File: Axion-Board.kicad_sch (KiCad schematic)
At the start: 76 parts, among them J1 USB_C_Receptacle_USB2.0, J14 QE2B, J15 RGB2, J16 RGB1, J17 QE1, J18 QE2, J19 USB Header, J2 SWD, J20 PS2 Header, J21 QE2A, J3 QE1A, J4 QE1B, J5 LED, J6 GPIO, J7 GPIO, Q1 BSS138, Q10 BSS138, Q11 BSS138, Q2 BSS138, Q3 BSS138, Q4 BSS138, Q5 BSS138, Q6 BSS138, Q7 BSS138, Q8 BSS138, Q9 BSS138, SW1 SW_Push, U1 W25Q128JVS, U2 USBLC6-2SC6, U3 RP2040, U4 XC6206PxxxMR-Regulator_Linear, U5 SN74HCT125DR, U6 78M05_TO252-3, Y1 12MHz

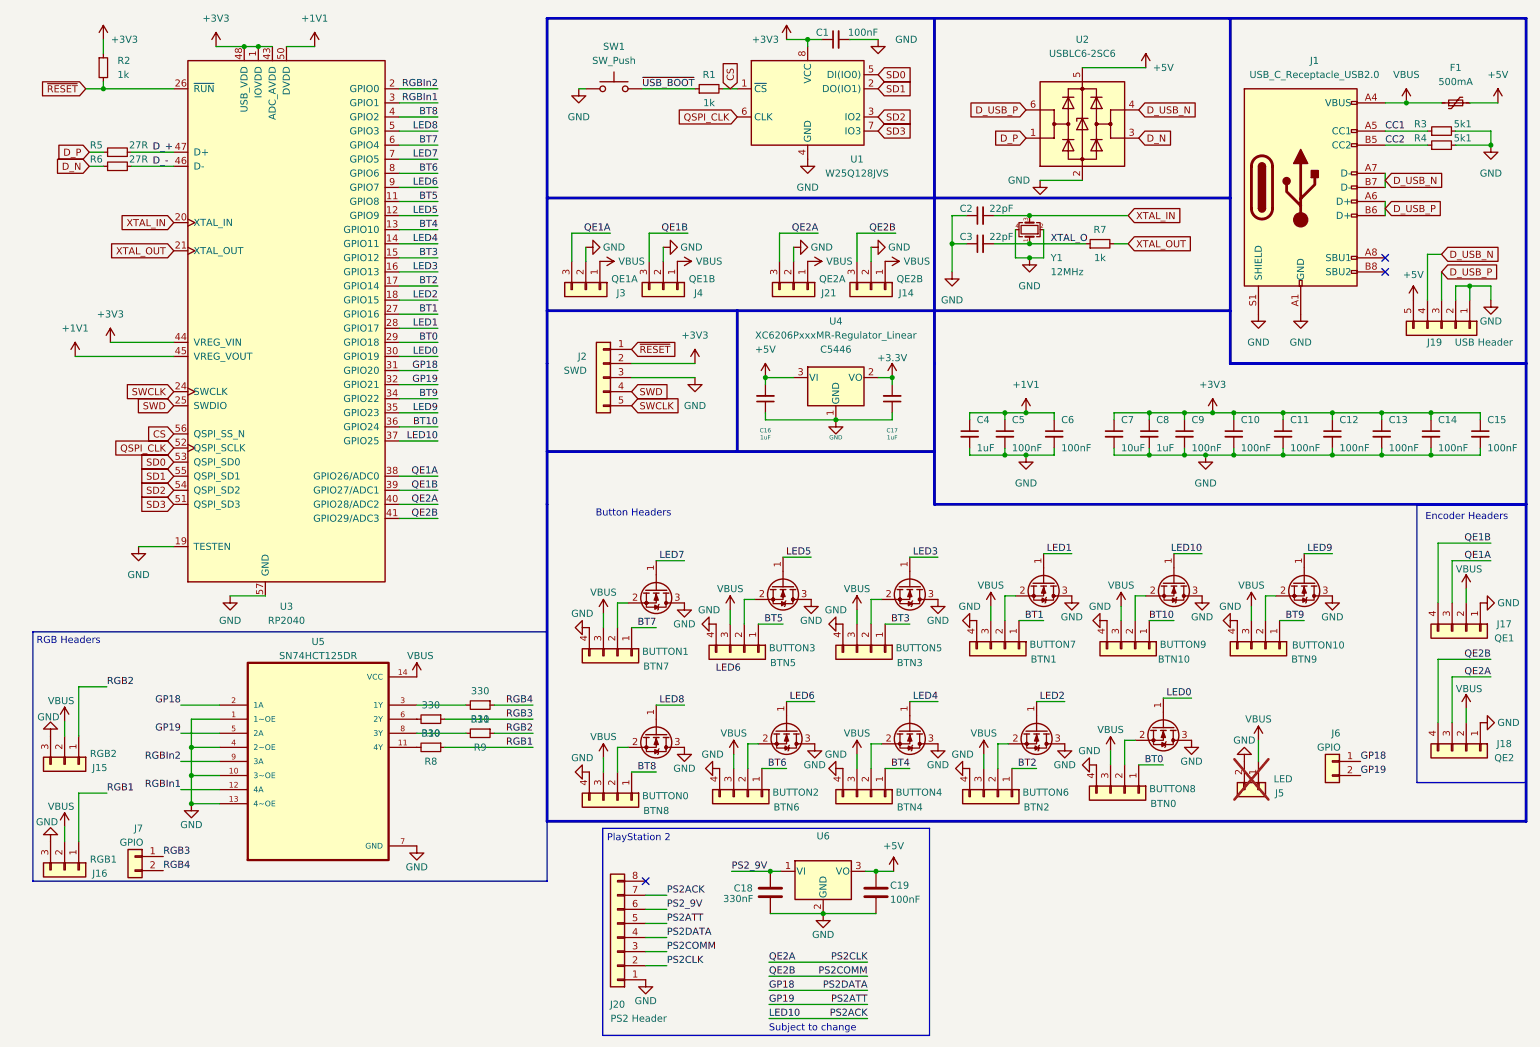
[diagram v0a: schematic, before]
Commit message: Fixed the mosfet wiring
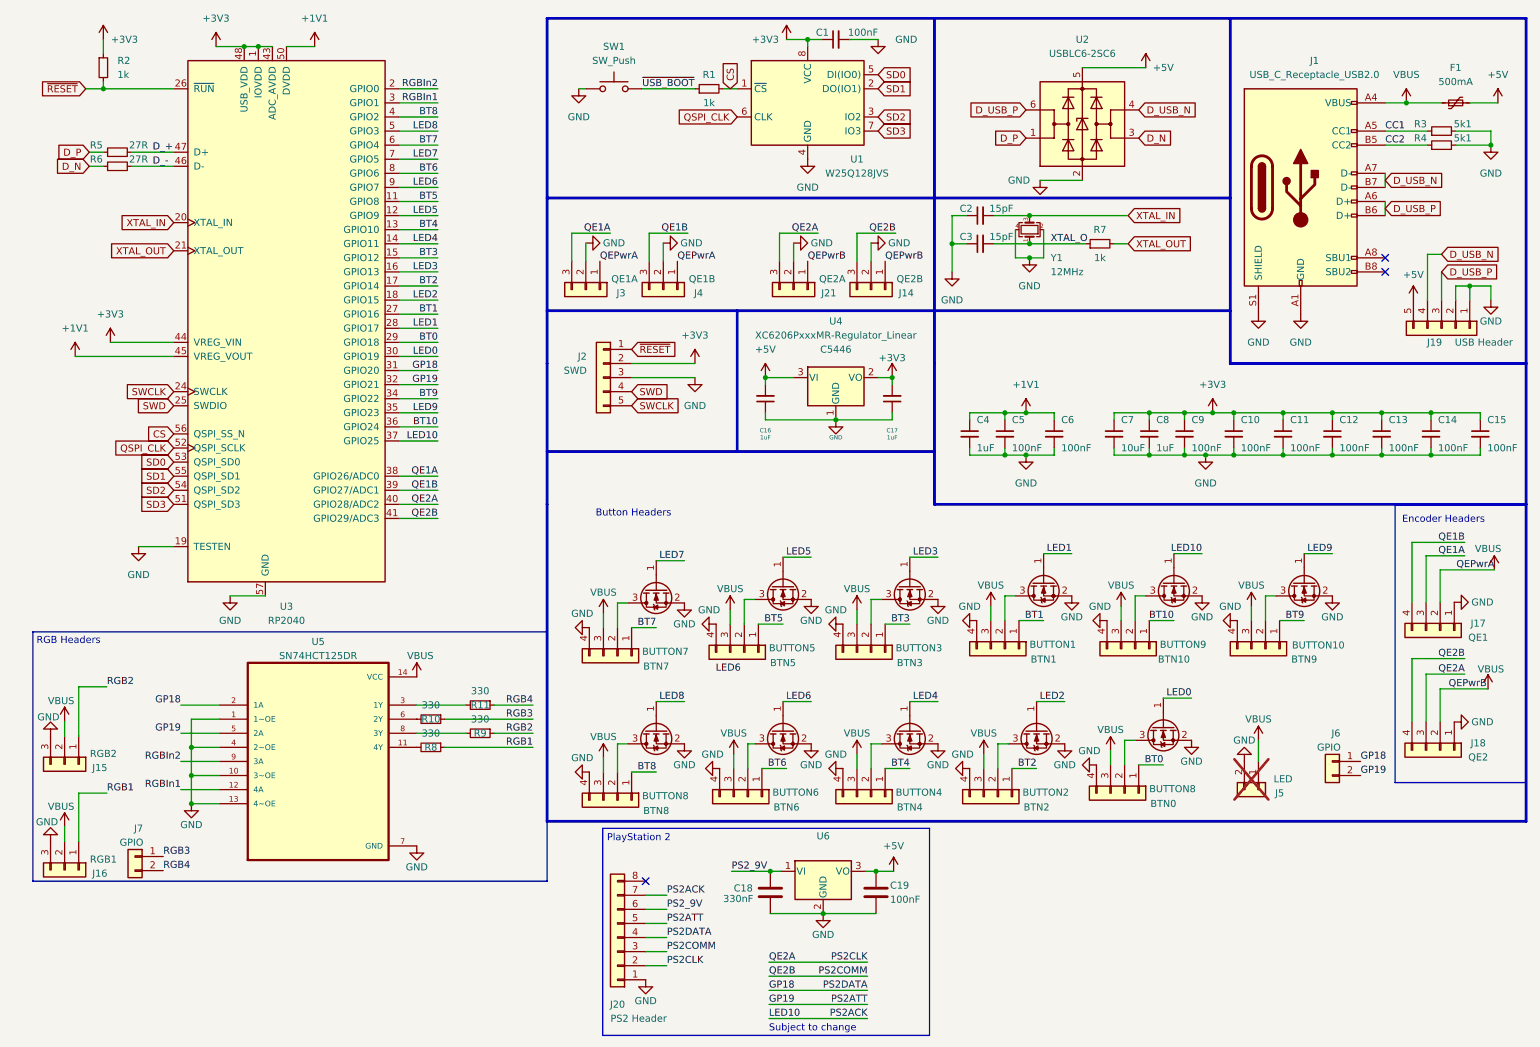
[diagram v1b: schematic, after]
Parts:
- BTN1: value BUTTON7 -> BUTTON1
- BTN2: value BUTTON6 -> BUTTON2
- BTN3: value BUTTON5 -> BUTTON3
- BTN5: value BUTTON3 -> BUTTON5
- BTN6: value BUTTON2 -> BUTTON6
- BTN7: value BUTTON1 -> BUTTON7
- BTN8: value BUTTON0 -> BUTTON8
- C2, C3: value 22pF -> 15pF
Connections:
- net GND: now also Q1.2 (S), Q10.2 (S), Q11.2 (S), Q2.2 (S), Q3.2 (S), Q4.2 (S), Q5.2 (S), Q6.2 (S), Q7.2 (S), Q8.2 (S), Q9.2 (S); no longer J1.B1 (GND), J1.B12 (GND), Q1.3 (D), Q10.3 (D), Q11.3 (D), Q2.3 (D), Q3.3 (D), Q4.3 (D), Q5.3 (D), Q6.3 (D), Q7.3 (D), Q8.3 (D), Q9.3 (D)
- net LED0: now also Q5.1 (G); no longer Q10.1 (G)
- net LED1: now also Q8.1 (G); no longer Q7.1 (G)
- net LED10: now also Q7.1 (G); no longer Q9.1 (G)
- net LED2: now also Q4.1 (G); no longer Q8.1 (G)
- net LED3: now also Q9.1 (G); no longer Q5.1 (G)
- net LED4: now also Q2.1 (G); no longer Q6.1 (G)
- net LED5: now also Q10.1 (G); no longer Q4.1 (G)
- net LED6: now also Q1.1 (G); no longer Q2.1 (G)
- net LED7: now also Q11.1 (G); no longer Q1.1 (G)
- net LED9: now also Q6.1 (G); no longer Q11.1 (G)
- net at BTN0.2 (Pin_2): now also Q5.3 (D); no longer Q10.2 (S)
- net at BTN9.2 (Pin_2): now also Q6.3 (D); no longer Q11.2 (S)
- net at BTN2.2 (Pin_2): now also Q4.3 (D); no longer Q8.2 (S)
- net at BTN5.2 (Pin_2): now also Q10.3 (D); no longer Q4.2 (S)
- net at BTN6.2 (Pin_2): now also Q1.3 (D); no longer Q2.2 (S)
- net at BTN8.2 (Pin_2): now also Q3.3 (D); no longer Q3.2 (S)
- net at BTN10.2 (Pin_2): now also Q7.3 (D); no longer Q9.2 (S)
- net at BTN4.2 (Pin_2): now also Q2.3 (D); no longer Q6.2 (S)
- net at BTN1.2 (Pin_2): now also Q8.3 (D); no longer Q7.2 (S)
- net at BTN7.2 (Pin_2): now also Q11.3 (D); no longer Q1.2 (S)
- net at BTN3.2 (Pin_2): now also Q9.3 (D); no longer Q5.2 (S)
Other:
- moved on the sheet: J17, J18

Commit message: Added turntable LED header
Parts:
- added J8: LED, Connector_JST:JST_XH_B2B-XH-A_1x02_P2.50mm_Vertical, symbol Connector_Generic:Conn_01x05
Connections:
- net GND: now also J8.1 (Pin_1)
- net VBUS: now also J8.2 (Pin_2)
- net GP18 renamed GP20
- net GP19 renamed GP21
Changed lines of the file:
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@@
 	(wire
 		(pts
+			(xy 97.155 156.845) (xy 97.155 159.385)
+		)
+		(stroke
+			(width 0)
+			(type default)
+		)
+	)
+	(wire
+		(pts
 			(xy 153.035 17.78) (xy 155.575 17.78)
 		)
@@
 		)
 	)
-	(label "GP19"
+	(label "GP21"
 		(at 86.36 80.01 180)
 		(fields_autoplaced yes)
@@
 		)
 	)
-	(label "GP19"
+	(label "GP21"
 		(at 252.73 150.495 0)
 		(fields_autoplaced yes)
@@
 		)
 	)
-	(label "GP19"
+	(label "GP21"
 		(at 40.005 142.875 180)
 		(fields_autoplaced yes)
@@
 		)
 	)
-	(label "GP18"
+	(label "GP20"
 		(at 252.73 147.955 0)
 		(fields_autoplaced yes)
@@
 		)
 	)
-	(label "GP18"
+	(label "GP20"
 		(at 86.36 77.47 180)
 		(fields_autoplaced yes)
@@
 		)
 	)
-	(label "GP18"
+	(label "GP20"
 		(at 146.05 189.23 0)
 		(fields_autoplaced yes)
@@
 		)
 	)
-	(label "GP19"
+	(label "GP21"
 		(at 146.05 191.77 0)
 		(fields_autoplaced yes)
@@
 		)
 	)
-	(label "GP18"
+	(label "GP20"
 		(at 40.005 137.795 180)
 		(fields_autoplaced yes)
@@
 	)
 	(symbol
+		(lib_id "power:GND")
+		(at 94.615 159.385 180)
+		(unit 1)
+		(exclude_from_sim no)
+		(in_bom yes)
+		(on_board yes)
+		(dnp no)
+		(property "Reference" "#PWR077"
+			(at 94.615 153.035 0)
+			(effects
+				(font
+					(size 1.27 1.27)
+				)
+				(hide yes)
+			)
+		)
+		(property "Value" "GND"
+			(at 94.234 155.956 0)
+			(effects
+				(font
+					(size 1.27 1.27)
+				)
+			)
+		)
+		(property "Footprint" ""
+			(at 94.615 159.385 0)
+			(effects
+				(font
+					(size 1.27 1.27)
+				)
+				(hide yes)
+			)
+		)
+		(property "Datasheet" ""
+			(at 94.615 159.385 0)
+			(effects
+				(font
+					(size 1.27 1.27)
+				)
+				(hide yes)
+			)
+		)
+		(property "Description" ""
+			(at 94.615 159.385 0)
+			(effects
+				(font
+					(size 1.27 1.27)
+				)
+				(hide yes)
+			)
+		)
+		(pin "1"
+		)
+		(instances
+			(project "Axion-Board"
+				(path "/ba62e47e-9e07-4e97-ab08-24b670d50f97"
+					(reference "#PWR077")
+					(unit 1)
+				)
+			)
+		)
+	)
+	(symbol
 		(lib_id "Device:C_Small")
 		(at 158.115 17.78 90)
@@
 	)
 	(symbol
+		(lib_id "power:VBUS")
+		(at 97.155 156.845 0)
+		(unit 1)
+		(exclude_from_sim no)
+		(in_bom yes)
+		(on_board yes)
+		(dnp no)
+		(property "Reference" "#PWR080"
+			(at 97.155 160.655 0)
+			(effects
+				(font
+					(size 1.27 1.27)
+				)
+				(hide yes)
+			)
+		)
+		(property "Value" "VBUS"
+			(at 96.52 153.162 0)
+			(effects
+				(font
+					(size 1.27 1.27)
+				)
+			)
+		)
+		(property "Footprint" ""
+			(at 97.155 156.845 0)
+			(effects
+				(font
+					(size 1.27 1.27)
+				)
+				(hide yes)
+			)
+		)
+		(property "Datasheet" ""
+			(at 97.155 156.845 0)
+			(effects
+				(font
+					(size 1.27 1.27)
+				)
+				(hide yes)
+			)
+		)
+		(property "Description" ""
+			(at 97.155 156.845 0)
+			(effects
+				(font
+					(size 1.27 1.27)
+				)
+				(hide yes)
+			)
+		)
+		(pin "1"
+		)
+		(instances
+			(project "Axion-Board"
+				(path "/ba62e47e-9e07-4e97-ab08-24b670d50f97"
+					(reference "#PWR080")
+					(unit 1)
+				)
+			)
+		)
+	)
+	(symbol
 		(lib_id "power:GND")
 		(at 150.495 54.483 90)
@@
 					(unit 1)
 				)
+			)
+		)
+	)
+	(symbol
+		(lib_name "Conn_01x05_1")
+		(lib_id "Connector_Generic:Conn_01x05")
+		(at 99.695 164.465 90)
+		(mirror x)
+		(unit 1)
+		(exclude_from_sim no)
+		(in_bom no)
+		(on_board yes)
+		(dnp no)
+		(property "Reference" "J8"
+			(at 100.33 164.465 90)
+			(effects
+				(font
+					(size 1.27 1.27)
+				)
+			)
+		)
+		(property "Value" "LED"
+			(at 101.6 161.925 90)
+			(effects
+				(font
+					(size 1.27 1.27)
+				)
+			)
+		)
+		(property "Footprint" "Connector_JST:JST_XH_B2B-XH-A_1x02_P2.50mm_Vertical"
+			(at 99.695 164.465 0)
+			(effects
+				(font
+					(size 1.27 1.27)
+				)
+				(hide yes)
+			)
+		)
+		(property "Datasheet" "~"
+			(at 99.695 164.465 0)
+			(effects
+				(font
+					(size 1.27 1.27)
+				)
+				(hide yes)
+			)
+		)
+		(property "Description" ""
+			(at 99.695 164.465 0)
+			(effects
+				(font
+					(size 1.27 1.27)
+				)
+				(hide yes)
+			)
+		)
+		(pin "1"
+		)
+		(pin "2"
+		)
+		(instances
+			(project "Axion-Board"
+				(path "/ba62e47e-9e07-4e97-ab08-24b670d50f97"
+					(reference "J8")
+					(unit 1)
+				)

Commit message: Added turntable LED header with BOM part
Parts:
- J8: LCSC (none) -> C158012
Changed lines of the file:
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@@
+			)
+		)
+		(property "LCSC" "C158012"
+			(at 99.695 164.465 90)
+			(effects
+				(font
+					(size 1.27 1.27)
+				)
+				(hide yes)
 			)
 		)
